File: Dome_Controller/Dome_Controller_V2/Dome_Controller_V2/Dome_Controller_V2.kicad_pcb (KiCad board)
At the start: 4 copper layers, 107 x 57 mm, 41 parts, among them J1 USB_B_Micro, J10 Conn_01x03, J11 Conn_02x04_Odd_Even, J12 Conn_01x04, J13 DB25_Female_MountingHoles, J14 DC-005-5A-2.0, J2 Servo Header, J3 Conn_02x03_Odd_Even, J4 Conn_01x03, J5 12IN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

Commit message: Added a lot since last check in
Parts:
- removed the G*** at (51.0, 83.7)
- removed the G*** at (51.0, 66.7)
- removed J2: Servo Header, Connector_PinHeader_2.54mm:PinHeader_1x06_P2.54mm_Vertical
- removed J3: Conn_02x03_Odd_Even, Connector_PinHeader_2.54mm:PinHeader_2x03_P2.54mm_Vertical
- removed the REF** at (50.0, 57.0)
- removed the REF** at (50.0, 103.0)
- removed the REF** at (148.0, 103.0)
- removed the REF** at (148.0, 57.0)
- added G***: LOGO, Logos:R2_Logo_V2, F.Cu at (50.3, 97.1)
- added G***: LOGO, Logos:R2_Logo_V2, F.Cu at (50.3, 68.6)
- added G***: LOGO, Logos:Dome_Controller_V2, F.Cu at (50.8, 82.6)
- added J16: RadarEye, Connector_Molex:Molex_KK-254_AE-6410-03A_1x03_P2.54mm_Vertical, F.Cu at (138.3, 101.9)
- added REF**: MountingHole_3.2mm_M3, MountingHole:MountingHole_3.2mm_M3, F.Cu at (48.8, 106.2)
- added REF**: MountingHole_3.2mm_M3, MountingHole:MountingHole_3.2mm_M3, F.Cu at (48.8, 56.8)
- added REF**: MountingHole_3.2mm_M3, MountingHole:MountingHole_3.2mm_M3, F.Cu at (149.0, 106.2)
- added REF**: MountingHole_3.2mm_M3, MountingHole:MountingHole_3.2mm_M3, F.Cu at (149.0, 56.8)
- added U7: PCA9685, Custom:PCA9685, F.Cu at (165.5, 81.0)
- J10: value Conn_01x03 -> SERIAL_PSI; footprint Connector_PinHeader_2.54mm:PinHeader_1x03_P2.54mm_Vertical -> Connector_Molex:Molex_KK-254_AE-6410-03A_1x03_P2.54mm_Vertical
- J11: value Conn_02x04_Odd_Even -> SERIAL_FU; footprint Connector_PinHeader_2.54mm:PinHeader_2x04_P2.54mm_Vertical -> Connector_Molex:Molex_KK-254_AE-6410-03A_1x03_P2.54mm_Vertical
- J12: value Conn_01x04 -> SERIAL_HP; footprint Connector_PinHeader_2.54mm:PinHeader_1x04_P2.54mm_Vertical -> Connector_Molex:Molex_KK-254_AE-6410-03A_1x03_P2.54mm_Vertical
- J4: value Conn_01x03 -> SERIAL_RS; footprint Connector_PinHeader_2.54mm:PinHeader_1x03_P2.54mm_Vertical -> Connector_Molex:Molex_KK-254_AE-6410-03A_1x03_P2.54mm_Vertical
- J8: value HP Servo -> 5V Out 2
- moved REF** 72.4 mm to (164.6, 76.8)
- moved U5 30.3 mm to (131.9, 94.4)
- moved C1 30.2 mm to (134.3, 95.3)
- moved C6 27.7 mm to (127.8, 90.0), turned to 180 degrees
- moved R1 22.5 mm to (123.8, 103.4)
- moved U2 20.8 mm to (102.6, 92.9), turned to 180 degrees
- moved U4 20.6 mm to (125.6, 96.1)
- moved R2 14.3 mm to (105.8, 89.3)
- moved L1 11.8 mm to (115.9, 96.2)
- moved R4 11.8 mm to (114.3, 93.6), turned to 0 degrees
- moved J4 11.0 mm to (138.3, 81.7), turned to 0 degrees
- moved C4 11.0 mm to (120.1, 95.6), turned to 180 degrees
- moved J12 9.35 mm to (138.3, 71.6), turned to 0 degrees
- moved C5 9.35 mm to (101.2, 89.3), turned to 0 degrees
- moved CR1 9.03 mm to (103.2, 86.7)
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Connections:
- J10 pad 2: RX_FU -> +5V
- J10 pad 3: TX_FU -> TX_PSI
- J11 pad 1: +5V -> GND
- J11 pad 2: +5V -> RX_FU
- J11 pad 3: GND -> TX_FU
- J12 pad 1: +5V -> GND
- J12 pad 2: GND -> RX_HP
- J12 pad 3: SR_SER_TX -> TX_HP
- J13 pad 19: SR_I2C_DATA -> D+
- J13 pad 20: +5V -> unconnected-(J13-Pad20)
- J13 pad 21: SR_SER_TX -> unconnected-(J13-Pad21)
- J13 pad 5: +5V -> VBUS
- J13 pad 6: SR_I2C_CLK -> D-
- J13 pad 8: GND -> unconnected-(J13-Pad8)
- J13 pad 9: SR_SER_RX -> unconnected-(J13-Pad9)
- J4 pad 2: +5V -> RX_RS
- J4 pad 3: CL_D -> TX_RS
- U1 pad 10: RX_RS -> unconnected-(U1-Pad10)
- U1 pad 11: TX_RS -> unconnected-(U1-Pad11)
- U1 pad 12: CL_D -> unconnected-(U1-Pad12)
- U1 pad 13: TX_FU -> unconnected-(U1-Pad13)
- U1 pad 14: RX_FU -> unconnected-(U1-Pad14)
- U1 pad 16: unconnected-(U1-Pad16) -> TX_PSI
- U1 pad 23: RX_HP -> TX_RS
- U1 pad 26: unconnected-(U1-Pad26) -> ST_LED_D
- U1 pad 27: TX_HP -> RX_RS
- U1 pad 28: unconnected-(U1-Pad28) -> TX_FU
- U1 pad 30: ST_LED_D -> RX_FU
- U1 pad 37: unconnected-(U1-Pad37) -> CL_D
- U1 pad 8: unconnected-(U1-Pad8) -> TX_HP
- U1 pad 9: unconnected-(U1-Pad9) -> RX_HP
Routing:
- net SR_SER_TX: track 124.7 -> 0.00 mm
- net SR_SER_RX: track 116.4 -> 0.00 mm
- net SR_I2C_DATA: track 109.3 -> 0.00 mm
- net SR_I2C_CLK: track 108.7 -> 0.00 mm
- net +12V: track 104.0 -> 0.00 mm
- net +5V: track 203.4 -> 106.1 mm, vias 1 -> 8
- net +3.3V: track 112.9 -> 202.3 mm, vias 0 -> 3
- net SDA: track 30.0 -> 114.8 mm
- net SCL: track 29.7 -> 109.5 mm
- net D+: track 17.9 -> 86.3 mm, vias 2 -> 1
- net D-: track 15.6 -> 82.4 mm, vias 2 -> 1
- net TX_PSI: track 0.00 -> 44.9 mm, vias 0 -> 1
- net CL_D: track 36.9 -> 66.6 mm
- net GPIO0: track 38.9 -> 13.5 mm
- net RESET: track 42.1 -> 63.7 mm, vias 3 -> 2
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- added copper zone on F.Cu, net +12V
- added copper zone on F.Cu, net +5V
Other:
- board size 107 x 57 mm -> 136.5 x 70 mm
- board text added: "PSI"
- board text added: "SCL"
- board text added: "SDA"
- board text added: "V+"
- board text added: "VCC"
- board text removed: "ESP Serial"
- board text removed: "I2C"
- board text removed: "Serial"
- board text removed: "Servo Expander"
- board text removed: "Slip Ring"

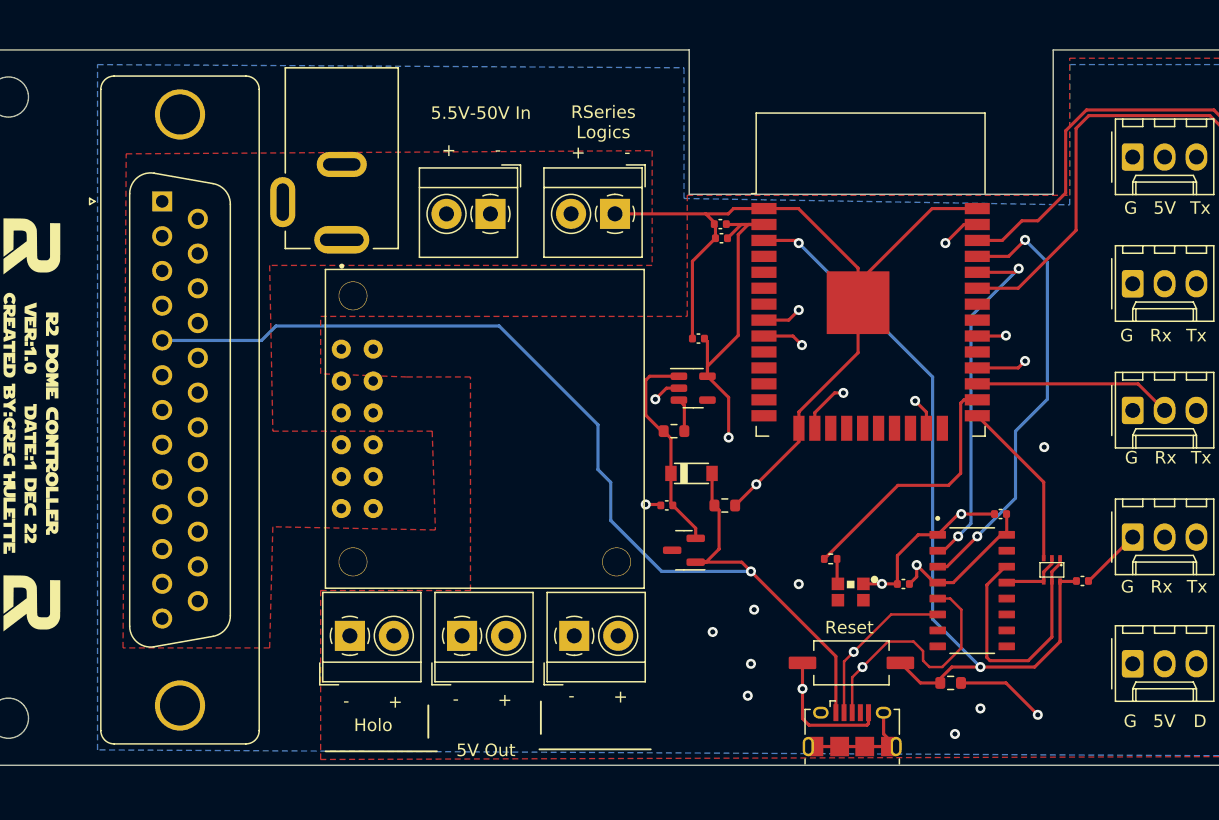
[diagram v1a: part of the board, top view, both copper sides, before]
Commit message: added LED PCBs
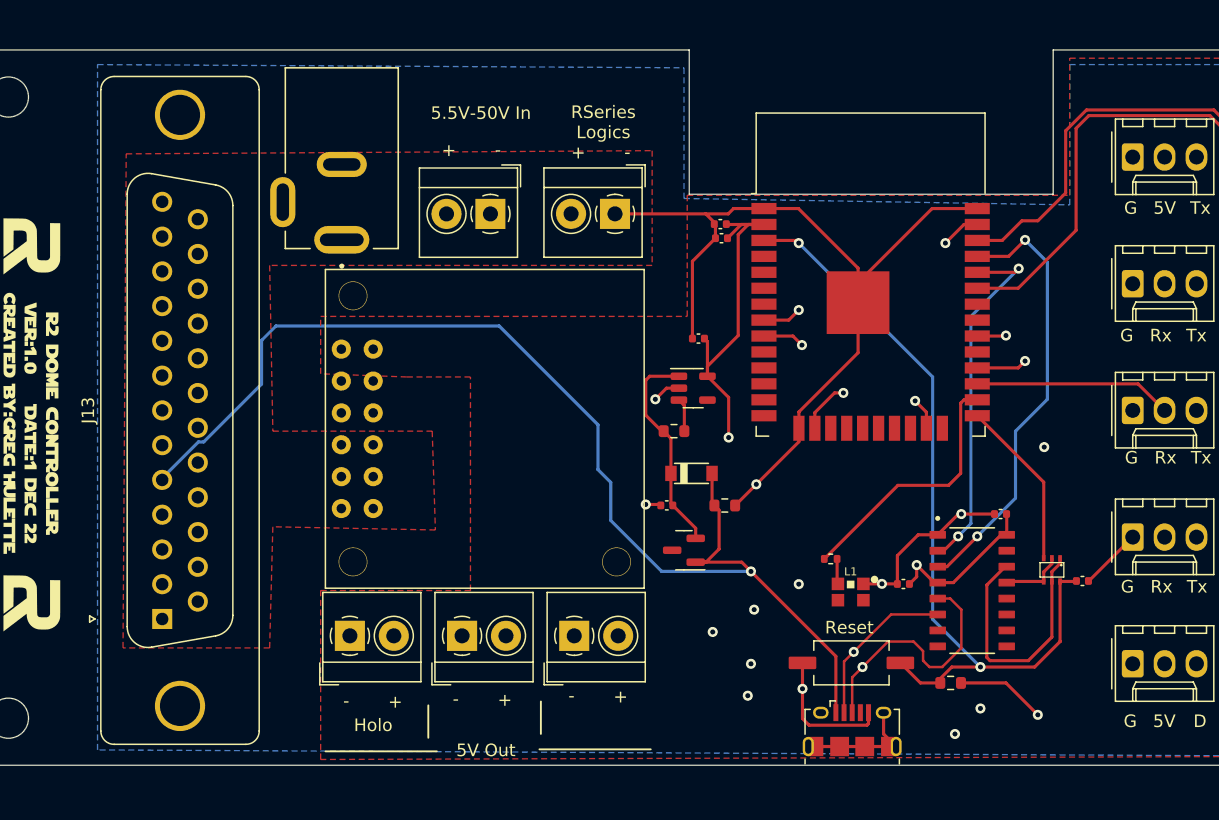
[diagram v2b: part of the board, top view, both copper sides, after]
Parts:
- J13: value DB25_Female_MountingHoles -> DB25_Male_MountingHoles; footprint Connector_Dsub:DSUB-25_Female_Vertical_P2.77x2.84mm_MountingHoles -> Connector_Dsub:DSUB-25_Male_Vertical_P2.77x2.84mm_MountingHoles
- moved J13 33.3 mm to (61.0, 98.3)
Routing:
- net VBUS: track 86.7 -> 93.4 mm
- net D+: track 86.3 -> 85.2 mm
- net D-: track 82.4 -> 81.3 mm
